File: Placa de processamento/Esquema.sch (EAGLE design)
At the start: 12 parts

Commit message: Atualização
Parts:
- removed IC1: (no value), v-reg:78LXX
- added IC2: (no value), v-reg:78XXL
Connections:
- net GND: now also IC2.GND; no longer IC1.GND
- net N$12: now also IC2.OUT; no longer IC1.OUT
- net N$7: now also IC2.IN; no longer IC1.IN
- net N$8: now also U$2.RXD; no longer U$2.TXD
- net N$9: now also U$2.TXD; no longer U$2.RXD
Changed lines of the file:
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@@
 <part name="U$9" library="CRD" library_urn="urn:adsk.eagle:library:39051337" deviceset="MPU6050" device="V1" package3d_urn="urn:adsk.eagle:package:39029071/8"/>
 <part name="U$11" library="ESP32-DEVKITV1" library_urn="urn:adsk.eagle:library:44018017" deviceset="ESP32DEVKITV1" device="" package3d_urn="urn:adsk.eagle:package:44018021/1"/>
-<part name="IC1" library="v-reg" library_urn="urn:adsk.eagle:library:409" deviceset="78LXX" device="" package3d_urn="urn:adsk.eagle:package:30346/1"/>
 <part name="FRAME1" library="frames" library_urn="urn:adsk.eagle:library:229" deviceset="A3L-LOC" device=""/>
+<part name="IC2" library="v-reg" library_urn="urn:adsk.eagle:library:409" deviceset="78XXL" device="" package3d_urn="urn:adsk.eagle:package:30361/1"/>
 </parts>
 <sheets>
@@
 <attribute name="NAME" x="44.45" y="22.86" size="1.27" layer="95" rot="R90"/>
 </instance>
-<instance part="IC1" gate="1" x="0" y="20.32" smashed="yes" rot="R90">
-<attribute name="NAME" x="7.62" y="22.86" size="1.778" layer="95" rot="R90"/>
-<attribute name="VALUE" x="10.16" y="22.86" size="1.778" layer="96" rot="R90"/>
-</instance>
 <instance part="FRAME1" gate="G$1" x="-119.38" y="-109.22" smashed="yes">
 <attribute name="DRAWING_NAME" x="224.79" y="-93.98" size="2.54" layer="94"/>
 <attribute name="LAST_DATE_TIME" x="224.79" y="-99.06" size="2.286" layer="94"/>
 <attribute name="SHEET" x="238.125" y="-104.14" size="2.54" layer="94"/>
+</instance>
+<instance part="IC2" gate="A" x="-22.86" y="20.32" smashed="yes" rot="R90">
+<attribute name="NAME" x="-15.24" y="22.86" size="1.778" layer="95" rot="R90"/>
+<attribute name="VALUE" x="-12.7" y="22.86" size="1.778" layer="96" rot="R90"/>
 </instance>
 </instances>
@@
 <net name="N$8" class="0">
 <segment>
-<pinref part="U$2" gate="G$1" pin="TXD"/>
-<wire x1="0" y1="-7.62" x2="7.62" y2="-7.62" width="0.1524" layer="91"/>
-<wire x1="7.62" y1="-7.62" x2="7.62" y2="-22.86" width="0.1524" layer="91"/>
+<wire x1="7.62" y1="-10.16" x2="7.62" y2="-22.86" width="0.1524" layer="91"/>
 <wire x1="7.62" y1="-22.86" x2="63.5" y2="-22.86" width="0.1524" layer="91"/>
 <pinref part="U$11" gate="G$1" pin="IO17"/>
 <wire x1="63.5" y1="-22.86" x2="63.5" y2="0" width="0.1524" layer="91"/>
+<pinref part="U$2" gate="G$1" pin="RXD"/>
+<wire x1="7.62" y1="-10.16" x2="0" y2="-10.16" width="0.1524" layer="91"/>
 </segment>
 </net>
 <net name="N$9" class="0">
 <segment>
-<pinref part="U$2" gate="G$1" pin="RXD"/>
-<wire x1="0" y1="-10.16" x2="5.08" y2="-10.16" width="0.1524" layer="91"/>
-<wire x1="5.08" y1="-10.16" x2="5.08" y2="-25.4" width="0.1524" layer="91"/>
+<wire x1="5.08" y1="-7.62" x2="5.08" y2="-25.4" width="0.1524" layer="91"/>
 <pinref part="U$11" gate="G$1" pin="IO16"/>
 <wire x1="5.08" y1="-25.4" x2="60.96" y2="-25.4" width="0.1524" layer="91"/>
 <wire x1="60.96" y1="-25.4" x2="60.96" y2="0" width="0.1524" layer="91"/>
+<pinref part="U$2" gate="G$1" pin="TXD"/>
+<wire x1="5.08" y1="-7.62" x2="0" y2="-7.62" width="0.1524" layer="91"/>
 </segment>
 </net>
@@
 <wire x1="22.86" y1="35.56" x2="48.26" y2="35.56" width="0.1524" layer="91"/>
 <wire x1="22.86" y1="12.7" x2="22.86" y2="35.56" width="0.1524" layer="91"/>
-<pinref part="IC1" gate="1" pin="IN"/>
-<wire x1="0" y1="12.7" x2="22.86" y2="12.7" width="0.1524" layer="91"/>
 <wire x1="48.26" y1="40.64" x2="48.26" y2="35.56" width="0.1524" layer="91"/>
 <junction x="48.26" y="35.56"/>
@@
 <wire x1="-29.21" y1="68.58" x2="-29.21" y2="73.66" width="0.1524" layer="91"/>
 <wire x1="-29.21" y1="73.66" x2="-2.54" y2="73.66" width="0.1524" layer="91"/>
+<pinref part="IC2" gate="A" pin="IN"/>
+<wire x1="22.86" y1="12.7" x2="-22.86" y2="12.7" width="0.1524" layer="91"/>
 </segment>
 </net>
 <net name="N$12" class="0">
 <segment>
-<pinref part="IC1" gate="1" pin="OUT"/>
 <wire x1="0" y1="27.94" x2="0" y2="30.48" width="0.1524" layer="91"/>
 <wire x1="0" y1="30.48" x2="-7.62" y2="30.48" width="0.1524" layer="91"/>
@@
 <wire x1="5.08" y1="10.16" x2="5.08" y2="-2.54" width="0.1524" layer="91"/>
 <wire x1="5.08" y1="-2.54" x2="0" y2="-2.54" width="0.1524" layer="91"/>
+<pinref part="IC2" gate="A" pin="OUT"/>
+<wire x1="0" y1="27.94" x2="-22.86" y2="27.94" width="0.1524" layer="91"/>
 </segment>
 </net>
@@
 <junction x="137.16" y="-15.24"/>
 <junction x="50.8" y="-15.24"/>
-<pinref part="IC1" gate="1" pin="GND"/>
 <wire x1="7.62" y1="20.32" x2="7.62" y2="-5.08" width="0.1524" layer="91"/>
 <wire x1="7.62" y1="-5.08" x2="50.8" y2="-5.08" width="0.1524" layer="91"/>
@@
 <wire x1="30.48" y1="-27.94" x2="30.48" y2="-15.24" width="0.1524" layer="91"/>
 <wire x1="30.48" y1="-15.24" x2="50.8" y2="-15.24" width="0.1524" layer="91"/>
-</segment>
-</net>
+<pinref part="IC2" gate="A" pin="GND"/>
+<wire x1="7.62" y1="20.32" x2="-15.24" y2="20.32" width="0.1524" layer="91"/>
+</segment>
+</net>

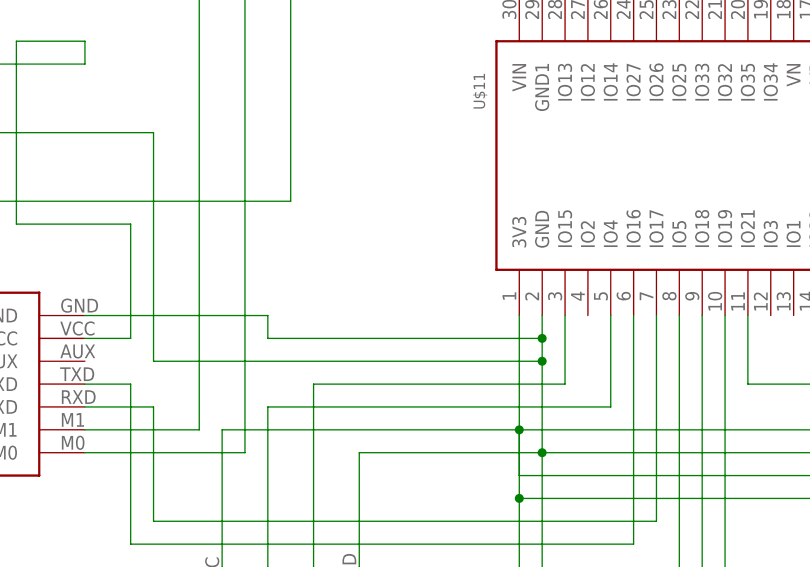
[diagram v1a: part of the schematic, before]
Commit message: Adicionado LED indicativo.
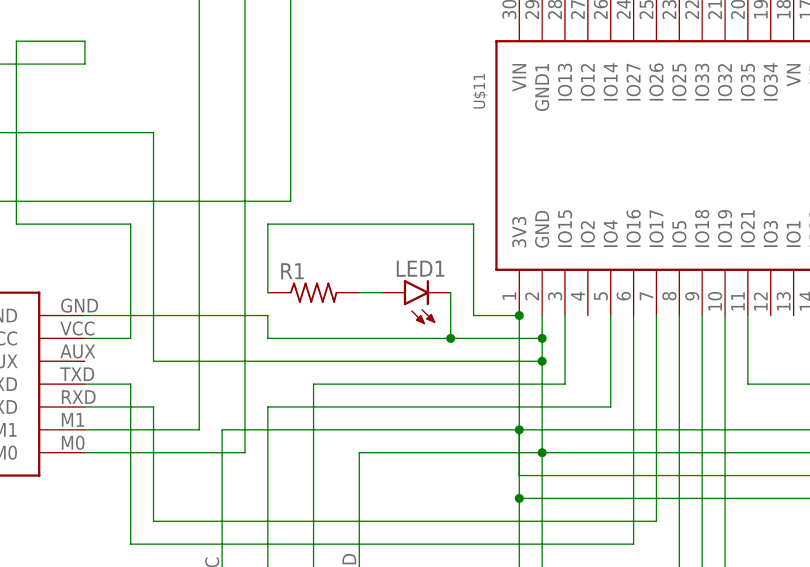
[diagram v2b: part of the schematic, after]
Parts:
- added LED1: (no value), led:LED5MM
- added R1: (no value), rcl:R-US_0309/12
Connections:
- new net N$4: LED1.A, R1.2
- net GND: now also LED1.C
- net N$3: now also R1.1
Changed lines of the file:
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@@
 <part name="FRAME1" library="frames" library_urn="urn:adsk.eagle:library:229" deviceset="A3L-LOC" device=""/>
 <part name="IC2" library="v-reg" library_urn="urn:adsk.eagle:library:409" deviceset="78XXL" device="" package3d_urn="urn:adsk.eagle:package:30361/1"/>
+<part name="LED1" library="led" library_urn="urn:adsk.eagle:library:259" deviceset="LED" device="5MM" package3d_urn="urn:adsk.eagle:package:15799/2"/>
+<part name="R1" library="rcl" library_urn="urn:adsk.eagle:library:334" deviceset="R-US_" device="0309/12" package3d_urn="urn:adsk.eagle:package:23571/1"/>
 </parts>
 <sheets>
@@
 <attribute name="VALUE" x="-12.7" y="22.86" size="1.778" layer="96" rot="R90"/>
 </instance>
+<instance part="LED1" gate="G$1" x="35.56" y="2.54" smashed="yes" rot="R90">
+<attribute name="NAME" x="40.132" y="6.096" size="1.778" layer="95" rot="R180"/>
+<attribute name="VALUE" x="40.132" y="8.255" size="1.778" layer="96" rot="R180"/>
+</instance>
+<instance part="R1" gate="G$1" x="25.4" y="2.54" smashed="yes">
+<attribute name="NAME" x="21.59" y="4.0386" size="1.778" layer="95"/>
+<attribute name="VALUE" x="21.59" y="-0.762" size="1.778" layer="96"/>
+</instance>
 </instances>
 <busses>
@@
 <wire x1="119.38" y1="-20.32" x2="48.26" y2="-20.32" width="0.1524" layer="91"/>
 <junction x="48.26" y="-20.32"/>
+<pinref part="R1" gate="G$1" pin="1"/>
+<wire x1="20.32" y1="2.54" x2="20.32" y2="10.16" width="0.1524" layer="91"/>
+<wire x1="20.32" y1="10.16" x2="43.18" y2="10.16" width="0.1524" layer="91"/>
+<wire x1="43.18" y1="10.16" x2="43.18" y2="0" width="0.1524" layer="91"/>
+<wire x1="43.18" y1="0" x2="48.26" y2="0" width="0.1524" layer="91"/>
+<junction x="48.26" y="0"/>
 </segment>
 </net>
@@
 <wire x1="20.32" y1="0" x2="20.32" y2="-2.54" width="0.1524" layer="91"/>
 <junction x="50.8" y="-2.54"/>
-<wire x1="20.32" y1="-2.54" x2="50.8" y2="-2.54" width="0.1524" layer="91"/>
+<wire x1="20.32" y1="-2.54" x2="40.64" y2="-2.54" width="0.1524" layer="91"/>
 <pinref part="U$3" gate="G$1" pin="GND"/>
+<wire x1="40.64" y1="-2.54" x2="50.8" y2="-2.54" width="0.1524" layer="91"/>
 <wire x1="30.48" y1="-27.94" x2="30.48" y2="-15.24" width="0.1524" layer="91"/>
 <wire x1="30.48" y1="-15.24" x2="50.8" y2="-15.24" width="0.1524" layer="91"/>
 <pinref part="IC2" gate="A" pin="GND"/>
 <wire x1="7.62" y1="20.32" x2="-15.24" y2="20.32" width="0.1524" layer="91"/>
+<pinref part="LED1" gate="G$1" pin="C"/>
+<wire x1="40.64" y1="2.54" x2="40.64" y2="-2.54" width="0.1524" layer="91"/>
+<junction x="40.64" y="-2.54"/>
+</segment>
+</net>
+<net name="N$4" class="0">
+<segment>
+<pinref part="R1" gate="G$1" pin="2"/>
+<pinref part="LED1" gate="G$1" pin="A"/>
+<wire x1="30.48" y1="2.54" x2="33.02" y2="2.54" width="0.1524" layer="91"/>
 </segment>
 </net>
@@
 packages will not be understood (or retained) with this version.
 </note>
+<note version="8.4" severity="warning">
+Since Version 8.4, EAGLE supports properties for SPICE simulation.
+Probes in schematics and SPICE mapping objects found in parts and library devices
+will not be understood with this version. Update EAGLE to the latest version
+for full support of SPICE simulation.
+</note>
 </compatibility>
